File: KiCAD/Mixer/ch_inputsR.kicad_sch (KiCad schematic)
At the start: 8 parts, among them J3 AudioJack2, Q1 NPN

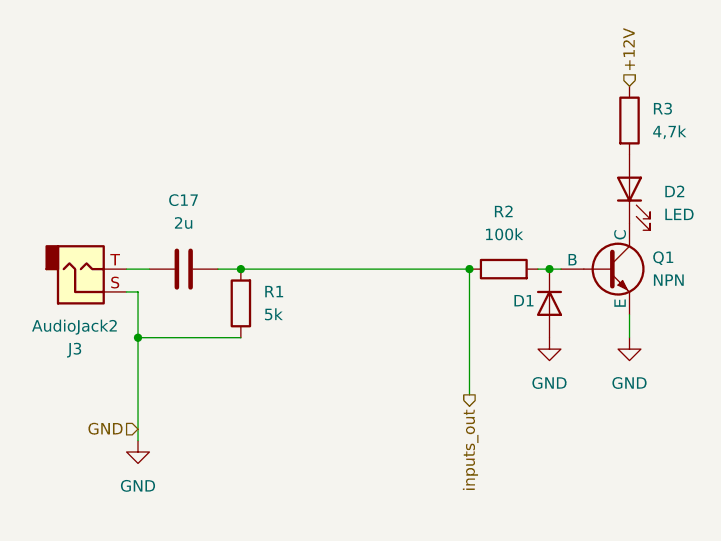
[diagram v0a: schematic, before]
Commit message: Rework of schematic, with error fixes and reworked pcb
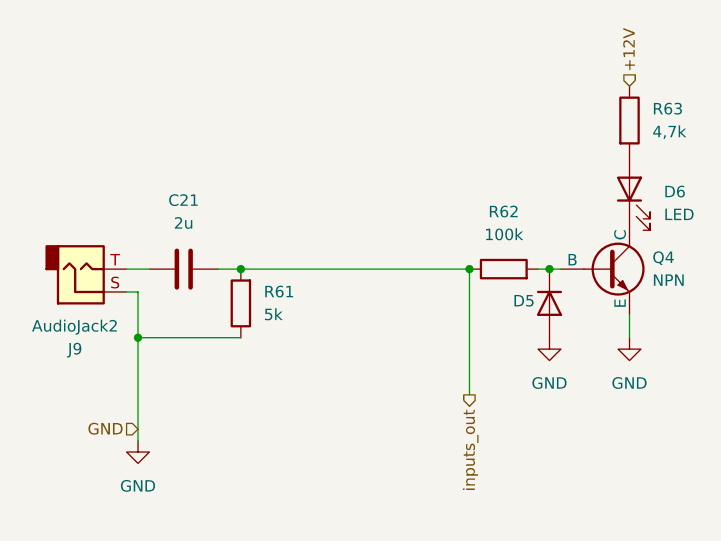
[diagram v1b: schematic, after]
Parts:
- renumbered C17 to C21, D1 to D5, D2 to D6, J3 to J9, Q1 to Q4, R1 to R61, R2 to R62, R3 to R63
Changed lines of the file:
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@@
 		(dnp no)
 		(fields_autoplaced yes)
-		(property "Reference" "#PWR011"
+		(property "Reference" "#PWR024"
 			(at 59.69 76.2 0)
 			(hide yes)
@@
 		(instances
 			(project "Mixer"
-				(path "/322d427a-6aae-4762-92d6-d97688daf29b/8a2849b7-184d-4014-bb98-da9dec8b5f90/ec5da5cc-7c1b-4e14-ac3c-00357a5f573e"
-					(reference "#PWR011")
+				(path "/322d427a-6aae-4762-92d6-d97688daf29b/8a2849b7-184d-4014-bb98-da9dec8b5f90/1134652d-8354-4f6a-9b2f-dc88b7881384"
+					(reference "#PWR024")
 					(unit 1)
 				)
@@
 		(dnp no)
 		(fields_autoplaced yes)
-		(property "Reference" "R3"
+		(property "Reference" "R63"
 			(at 116.84 33.02 0)
 			(show_name no)
@@
 		(instances
 			(project "Mixer"
-				(path "/322d427a-6aae-4762-92d6-d97688daf29b/8a2849b7-184d-4014-bb98-da9dec8b5f90/ec5da5cc-7c1b-4e14-ac3c-00357a5f573e"
-					(reference "R3")
+				(path "/322d427a-6aae-4762-92d6-d97688daf29b/8a2849b7-184d-4014-bb98-da9dec8b5f90/1134652d-8354-4f6a-9b2f-dc88b7881384"
+					(reference "R63")
 					(unit 1)
 				)
@@
 		(in_pos_files yes)
 		(dnp no)
-		(property "Reference" "J3"
+		(property "Reference" "J9"
 			(at 52.705 59.69 0)
 			(show_name no)
@@
 		(instances
 			(project "Mixer"
-				(path "/322d427a-6aae-4762-92d6-d97688daf29b/8a2849b7-184d-4014-bb98-da9dec8b5f90/ec5da5cc-7c1b-4e14-ac3c-00357a5f573e"
-					(reference "J3")
+				(path "/322d427a-6aae-4762-92d6-d97688daf29b/8a2849b7-184d-4014-bb98-da9dec8b5f90/1134652d-8354-4f6a-9b2f-dc88b7881384"
+					(reference "J9")
 					(unit 1)
 				)
@@
 		(dnp no)
 		(fields_autoplaced yes)
-		(property "Reference" "Q1"
+		(property "Reference" "Q4"
 			(at 116.84 49.53 0)
 			(show_name no)
@@
 		(instances
 			(project "Mixer"
-				(path "/322d427a-6aae-4762-92d6-d97688daf29b/8a2849b7-184d-4014-bb98-da9dec8b5f90/ec5da5cc-7c1b-4e14-ac3c-00357a5f573e"
-					(reference "Q1")
+				(path "/322d427a-6aae-4762-92d6-d97688daf29b/8a2849b7-184d-4014-bb98-da9dec8b5f90/1134652d-8354-4f6a-9b2f-dc88b7881384"
+					(reference "Q4")
 					(unit 1)
 				)
@@
 		(in_pos_files yes)
 		(dnp no)
-		(property "Reference" "D1"
+		(property "Reference" "D5"
 			(at 101.346 54.356 90)
 			(show_name no)
@@
 		(instances
 			(project "Mixer"
-				(path "/322d427a-6aae-4762-92d6-d97688daf29b/8a2849b7-184d-4014-bb98-da9dec8b5f90/ec5da5cc-7c1b-4e14-ac3c-00357a5f573e"
-					(reference "D1")
+				(path "/322d427a-6aae-4762-92d6-d97688daf29b/8a2849b7-184d-4014-bb98-da9dec8b5f90/1134652d-8354-4f6a-9b2f-dc88b7881384"
+					(reference "D5")
 					(unit 1)
 				)
@@
 		(dnp no)
 		(fields_autoplaced yes)
-		(property "Reference" "#PWR012"
+		(property "Reference" "#PWR025"
 			(at 105.41 64.77 0)
 			(hide yes)
@@
 		(instances
 			(project "Mixer"
-				(path "/322d427a-6aae-4762-92d6-d97688daf29b/8a2849b7-184d-4014-bb98-da9dec8b5f90/ec5da5cc-7c1b-4e14-ac3c-00357a5f573e"
-					(reference "#PWR012")
+				(path "/322d427a-6aae-4762-92d6-d97688daf29b/8a2849b7-184d-4014-bb98-da9dec8b5f90/1134652d-8354-4f6a-9b2f-dc88b7881384"
+					(reference "#PWR025")
 					(unit 1)
 				)
@@
 		(dnp no)
 		(fields_autoplaced yes)
-		(property "Reference" "R2"
+		(property "Reference" "R62"
 			(at 100.33 44.45 90)
 			(show_name no)
@@
 		(instances
 			(project "Mixer"
-				(path "/322d427a-6aae-4762-92d6-d97688daf29b/8a2849b7-184d-4014-bb98-da9dec8b5f90/ec5da5cc-7c1b-4e14-ac3c-00357a5f573e"
-					(reference "R2")
+				(path "/322d427a-6aae-4762-92d6-d97688daf29b/8a2849b7-184d-4014-bb98-da9dec8b5f90/1134652d-8354-4f6a-9b2f-dc88b7881384"
+					(reference "R62")
 					(unit 1)
 				)
@@
 		(dnp no)
 		(fields_autoplaced yes)
-		(property "Reference" "D2"
+		(property "Reference" "D6"
 			(at 118.11 42.2275 90)
 			(show_name no)
@@
 		(instances
 			(project "Mixer"
-				(path "/322d427a-6aae-4762-92d6-d97688daf29b/8a2849b7-184d-4014-bb98-da9dec8b5f90/ec5da5cc-7c1b-4e14-ac3c-00357a5f573e"
-					(reference "D2")
+				(path "/322d427a-6aae-4762-92d6-d97688daf29b/8a2849b7-184d-4014-bb98-da9dec8b5f90/1134652d-8354-4f6a-9b2f-dc88b7881384"
+					(reference "D6")
 					(unit 1)
 				)
@@
 		(dnp no)
 		(fields_autoplaced yes)
-		(property "Reference" "R1"
+		(property "Reference" "R61"
 			(at 73.66 53.34 0)
 			(show_name no)
@@
 		(instances
 			(project "Mixer"
-				(path "/322d427a-6aae-4762-92d6-d97688daf29b/8a2849b7-184d-4014-bb98-da9dec8b5f90/ec5da5cc-7c1b-4e14-ac3c-00357a5f573e"
-					(reference "R1")
+				(path "/322d427a-6aae-4762-92d6-d97688daf29b/8a2849b7-184d-4014-bb98-da9dec8b5f90/1134652d-8354-4f6a-9b2f-dc88b7881384"
+					(reference "R61")
 					(unit 1)
 				)
@@
 		(dnp no)
 		(fields_autoplaced yes)
-		(property "Reference" "C17"
+		(property "Reference" "C21"
 			(at 64.77 43.18 90)
 			(show_name no)
@@
 		(instances
 			(project "Mixer"
-				(path "/322d427a-6aae-4762-92d6-d97688daf29b/8a2849b7-184d-4014-bb98-da9dec8b5f90/ec5da5cc-7c1b-4e14-ac3c-00357a5f573e"
-					(reference "C17")
+				(path "/322d427a-6aae-4762-92d6-d97688daf29b/8a2849b7-184d-4014-bb98-da9dec8b5f90/1134652d-8354-4f6a-9b2f-dc88b7881384"
+					(reference "C21")
 					(unit 1)
 				)
@@
 		(dnp no)
 		(fields_autoplaced yes)
-		(property "Reference" "#PWR013"
+		(property "Reference" "#PWR026"
 			(at 114.3 64.77 0)
 			(hide yes)
@@
 		(instances
 			(project "Mixer"
-				(path "/322d427a-6aae-4762-92d6-d97688daf29b/8a2849b7-184d-4014-bb98-da9dec8b5f90/ec5da5cc-7c1b-4e14-ac3c-00357a5f573e"
-					(reference "#PWR013")
-					(unit 1)
-				)
+				(path "/322d427a-6aae-4762-92d6-d97688daf29b/8a2849b7-184d-4014-bb98-da9dec8b5f90/1134652d-8354-4f6a-9b2f-dc88b7881384"
+					(reference "#PWR026")
+					(unit 1)
+				)

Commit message: Final PCB Version that got ordered from JLCPCB
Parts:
- renumbered C21 to C25
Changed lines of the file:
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@@
 		(dnp no)
 		(fields_autoplaced yes)
-		(property "Reference" "#PWR024"
+		(property "Reference" "#PWR028"
 			(at 59.69 76.2 0)
 			(hide yes)
@@
 			(project "Mixer"
 				(path "/322d427a-6aae-4762-92d6-d97688daf29b/8a2849b7-184d-4014-bb98-da9dec8b5f90/1134652d-8354-4f6a-9b2f-dc88b7881384"
-					(reference "#PWR024")
+					(reference "#PWR028")
 					(unit 1)
 				)
@@
 		(dnp no)
 		(fields_autoplaced yes)
-		(property "Reference" "#PWR025"
+		(property "Reference" "#PWR029"
 			(at 105.41 64.77 0)
 			(hide yes)
@@
 			(project "Mixer"
 				(path "/322d427a-6aae-4762-92d6-d97688daf29b/8a2849b7-184d-4014-bb98-da9dec8b5f90/1134652d-8354-4f6a-9b2f-dc88b7881384"
-					(reference "#PWR025")
+					(reference "#PWR029")
 					(unit 1)
 				)
@@
 		(dnp no)
 		(fields_autoplaced yes)
-		(property "Reference" "C21"
+		(property "Reference" "C25"
 			(at 64.77 43.18 90)
 			(show_name no)
@@
 			(project "Mixer"
 				(path "/322d427a-6aae-4762-92d6-d97688daf29b/8a2849b7-184d-4014-bb98-da9dec8b5f90/1134652d-8354-4f6a-9b2f-dc88b7881384"
-					(reference "C21")
+					(reference "C25")
 					(unit 1)
 				)
@@
 		(dnp no)
 		(fields_autoplaced yes)
-		(property "Reference" "#PWR026"
+		(property "Reference" "#PWR030"
 			(at 114.3 64.77 0)
 			(hide yes)
@@
 			(project "Mixer"
 				(path "/322d427a-6aae-4762-92d6-d97688daf29b/8a2849b7-184d-4014-bb98-da9dec8b5f90/1134652d-8354-4f6a-9b2f-dc88b7881384"
-					(reference "#PWR026")
-					(unit 1)
-				)
+					(reference "#PWR030")
+					(unit 1)
+				)
